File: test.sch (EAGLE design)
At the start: 17 parts

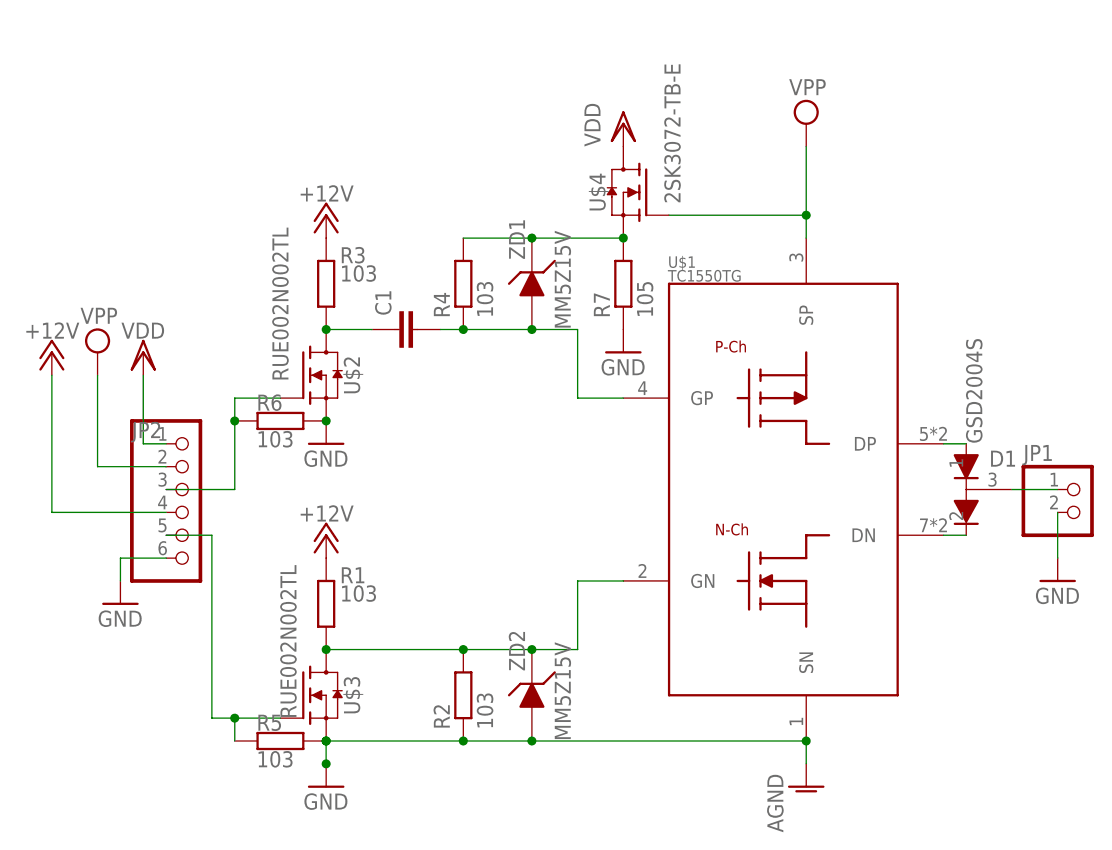
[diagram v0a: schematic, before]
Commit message: replace lower voltage FET by CMOS for putting off a CR circuit between HiVol-PMOS-Gate and 12V source.
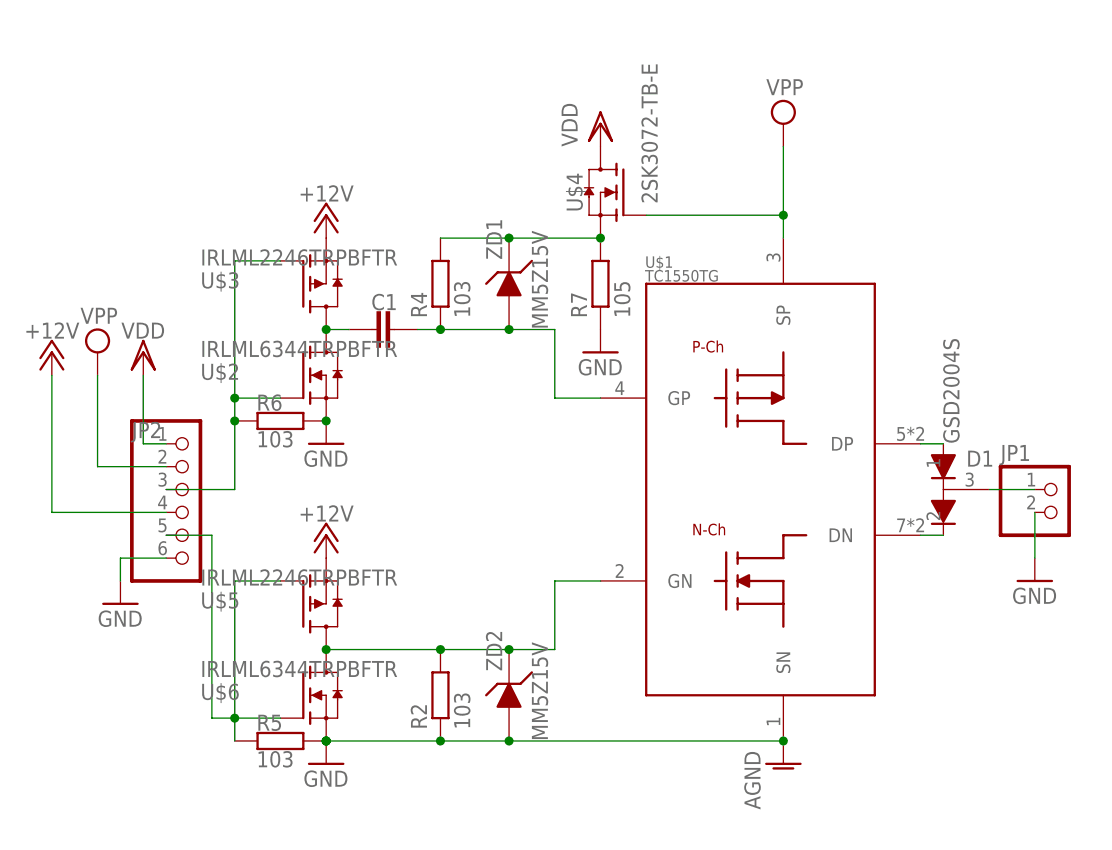
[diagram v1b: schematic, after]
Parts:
- removed R1, R3: 103, rcl:R-EU_0204/5
- added U$5: IRLML2246TRPBFTR, Transistor-FET:IRLML2246TRPBFTR
- added U$6: IRLML6344TRPBFTR, Transistor-FET:IRLML6344TRPBFTR
- U$2: value RUE002N002TL -> IRLML6344TRPBFTR; device Transistor-FET:RUE002N002TL -> Transistor-FET:IRLML6344TRPBFTR
- U$3: value RUE002N002TL -> IRLML2246TRPBFTR; device Transistor-FET:RUE002N002TL -> Transistor-FET:IRLML2246TRPBFTR
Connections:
- net +12V: now also U$3.S, U$5.S; no longer R1.2, R3.2
- net GND: now also U$6.S; no longer U$3.S
- net N$1: now also U$5.D, U$6.D; no longer R1.1, U$3.D
- net N$2: now also U$3.D; no longer R3.1
- net N$4: now also U$5.G, U$6.G; no longer U$3.G
- net N$5: now also U$3.G
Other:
- moved on the sheet: C1, D1, JP1, R2, R4, R7, U$1, U$4, ZD1, ZD2
